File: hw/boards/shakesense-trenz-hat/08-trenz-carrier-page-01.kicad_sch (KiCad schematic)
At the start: 8 parts, among them J83 1715721, J84 TSW-106-07-G-S, J85 TSW-103-07-G-D

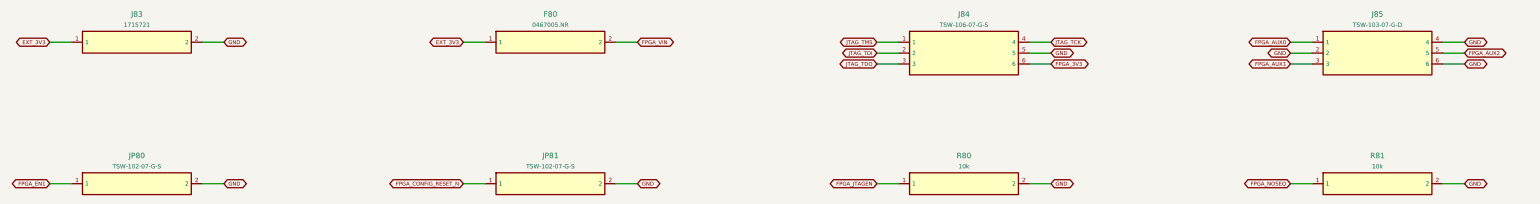
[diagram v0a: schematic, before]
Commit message: Expose Trenz GPIOs on the Pi-outline HDI sensor HAT
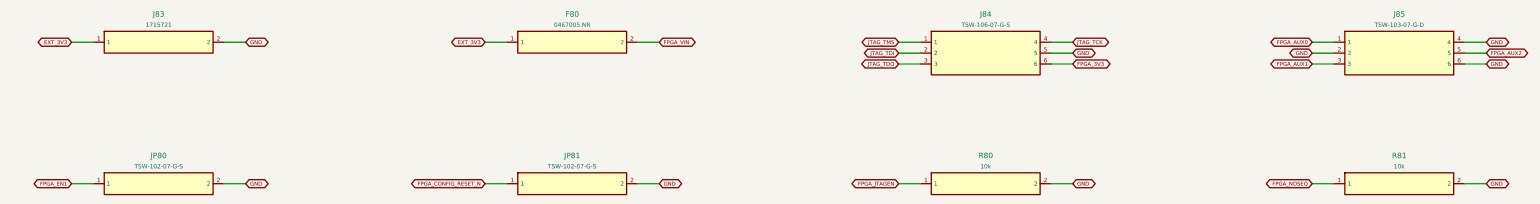
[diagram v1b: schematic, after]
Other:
- title: shakesense-trenz-hat / 08-trenz-carrier-page-01 -> ShakeSense T1 / 08-trenz-carrier-page-01
- moved on the sheet: F80, J83, J84, J85, JP80, JP81, R80, R81

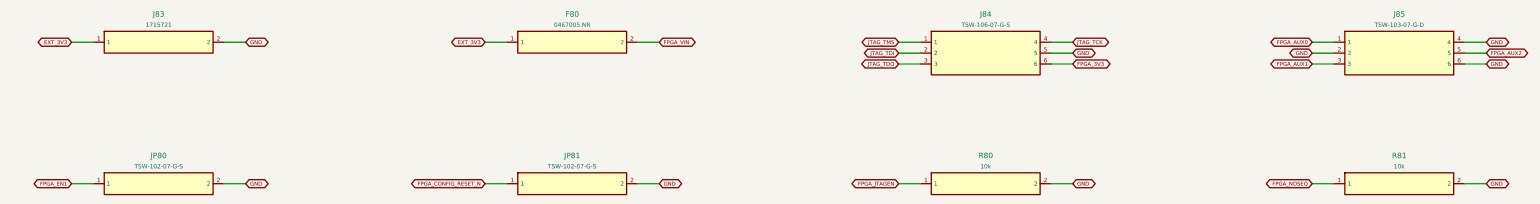
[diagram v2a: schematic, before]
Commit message: Implement internal Pi FPGA link and remove ribbon expansion
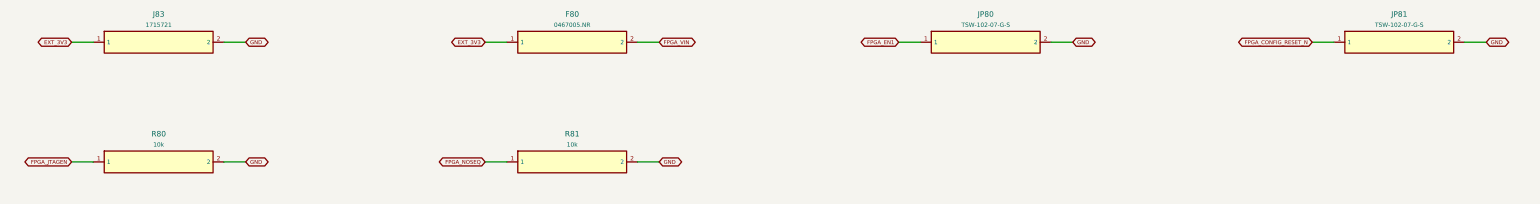
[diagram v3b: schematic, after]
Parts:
- removed J84: TSW-106-07-G-S, ShakeSense:TZ_TZ_JTAG, symbol ShakeSense:Part_J84
- removed J85: TSW-103-07-G-D, ShakeSense:TZ_TZ_AUX, symbol ShakeSense:Part_J85
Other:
- moved on the sheet: JP80, JP81, R80, R81
